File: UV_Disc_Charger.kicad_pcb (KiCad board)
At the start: 2 copper layers, 100 x 100 mm, 0 parts

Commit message: layout started
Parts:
- added C1: 10u, Capacitor_SMD:C_0805_2012Metric_Pad1.18x1.45mm_HandSolder, F.Cu at (242.0, 89.2)
- added C10: 100u, Capacitor_SMD:C_1206_3216Metric, F.Cu at (98.8, 170.2)
- added C11: 100n, Capacitor_SMD:C_0603_1608Metric_Pad1.08x0.95mm_HandSolder, F.Cu at (92.9, 173.8)
- added C2: 10u, Capacitor_SMD:C_0805_2012Metric_Pad1.18x1.45mm_HandSolder, F.Cu at (176.5, 76.2)
- added C3: 100n, Capacitor_SMD:C_0603_1608Metric_Pad1.08x0.95mm_HandSolder, F.Cu at (222.3, 86.4)
- added C4: 10u, Capacitor_SMD:C_0805_2012Metric, F.Cu at (98.2, 173.4)
- added C5: 10u, Capacitor_SMD:C_0805_2012Metric, F.Cu at (98.2, 176.4)
- added C6: 22u, Capacitor_SMD:C_1206_3216Metric, F.Cu at (98.8, 156.8)
- added C7: 22u, Capacitor_SMD:C_1206_3216Metric, F.Cu at (98.8, 160.2)
- added C8: 22u, Capacitor_SMD:C_1206_3216Metric, F.Cu at (98.8, 163.5)
- added C9: 22u, Capacitor_SMD:C_1206_3216Metric, F.Cu at (98.8, 166.9)
- added D1: SMBJ12CA, Diode_SMD:D_SMB, F.Cu at (167.6, 87.6)
- added D2: RED, Diode_SMD:D_0805_2012Metric, F.Cu at (185.4, 80.0)
- added D3: GREEN, Diode_SMD:D_0805_2012Metric, F.Cu at (183.5, 81.9)
- added D4: SS34, Diode_SMD:D_SMA, F.Cu at (163.8, 83.8)
- added F1: 1.5A, Fuse:Fuse_1206_3216Metric, F.Cu at (230.9, 51.4)
- added H1: MountingHole, MountingHole:MountingHole_3.2mm_M3_DIN965_Pad, F.Cu at (26.2, 109.8)
- added H2: MountingHole, MountingHole:MountingHole_3.2mm_M3_DIN965_Pad, F.Cu at (26.2, 117.0)
- added J1: Type-C_6P, Custom:USB-C 6 Pin - Long pads, F.Cu at (181.2, 91.1)
- added J2: JST PH Connector, Connector_JST:JST_PH_B2B-PH-K_1x02_P2.00mm_Vertical, F.Cu at (12.3, 133.7)
- added J3: Conn_01x01, Connector_PinHeader_2.54mm:PinHeader_1x01_P2.54mm_Vertical, F.Cu at (32.1, 108.5)
- added J4: JST PH Connector, Connector_JST:JST_PH_B2B-PH-K_1x02_P2.00mm_Vertical, F.Cu at (12.3, 140.3)
- added J5: JST PH Connector, Connector_PinHeader_2.54mm:PinHeader_1x02_P2.54mm_Vertical, F.Cu at (38.4, 122.8)
- added J6: JST PH Connector, Connector_PinHeader_2.54mm:PinHeader_1x02_P2.54mm_Vertical, F.Cu at (43.1, 122.8)
- added J7: Conn_01x01, Connector_PinHeader_2.54mm:PinHeader_1x01_P2.54mm_Vertical, F.Cu at (32.1, 113.2)
- added L1: 2u2, Custom:Combined CD43 + L 6.3x6.3, F.Cu at (105.5, 159.4)
- added Q1: SI2301, Package_TO_SOT_SMD:SOT-23, F.Cu at (237.5, 71.3)
- added Q2: SI2301, Package_TO_SOT_SMD:SOT-23, F.Cu at (243.0, 71.5)
- added R10: 1M6, Resistor_SMD:R_0805_2012Metric, F.Cu at (89.4, 148.2)
- added R11: 1M, Resistor_SMD:R_0805_2012Metric, F.Cu at (89.4, 151.2)
- added R12: 180k, Resistor_SMD:R_0805_2012Metric, F.Cu at (89.4, 154.1)
- added R13: 1k, Resistor_SMD:R_0805_2012Metric, F.Cu at (223.2, 57.4)
- added R14: 10k, Resistor_SMD:R_0805_2012Metric, F.Cu at (223.2, 60.3)
- added R15: 0R4, Resistor_SMD:R_0805_2012Metric, F.Cu at (174.0, 81.3)
- added R16: 2512 package, Resistor_SMD:R_2512_6332Metric, F.Cu at (174.0, 81.3)
- added R3: 100R, Resistor_SMD:R_0805_2012Metric, F.Cu at (214.3, 57.4)
- added R4: 1k, Resistor_SMD:R_0805_2012Metric, F.Cu at (181.0, 78.1)
- added R5: 1k, Resistor_SMD:R_0805_2012Metric, F.Cu at (214.3, 63.3)
- added R6: 5k1, Resistor_SMD:R_0805_2012Metric, F.Cu at (172.7, 94.0)
- added R7: 5k1, Resistor_SMD:R_0805_2012Metric, F.Cu at (170.2, 91.4)
- added R8: 1k, Resistor_SMD:R_0805_2012Metric, F.Cu at (182.9, 74.9)
- added R9: 2k, Resistor_SMD:R_0805_2012Metric, F.Cu at (185.4, 71.5)
- added U1: TP4056, Package_SO:SOP-8_3.76x4.96mm_P1.27mm, F.Cu at (179.1, 69.8)
- added U2: DW01A, Package_TO_SOT_SMD:SOT-23-6, F.Cu at (222.7, 82.9)
- added U3: FS8205A, Package_SO:TSSOP-8_4.4x3mm_P0.65mm, F.Cu at (241.5, 63.1)
- added U4: TPS63020, TPS63020:QFN14-3X4MM, F.Cu at (117.8, 166.3)
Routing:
- net Net-(D2-A): track 0.00 -> 31.4 mm
- net VBUS: track 0.00 -> 19.6 mm
- net Net-(D3-K): track 0.00 -> 13.7 mm
- net Net-(U1-CHRG): track 0.00 -> 10.4 mm, vias 0 -> 2
- net Net-(J1-CC2): track 0.00 -> 10.2 mm
- net Net-(J1-CC1): track 0.00 -> 10.0 mm
- net Net-(U1-STDBY): track 0.00 -> 9.66 mm, vias 0 -> 2
- net Net-(D2-K): track 0.00 -> 8.67 mm
- net Net-(U1-PROG): track 0.00 -> 3.84 mm
- net GND: track 0.00 -> 3.31 mm, vias 0 -> 2
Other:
- copper layers 2 -> 4

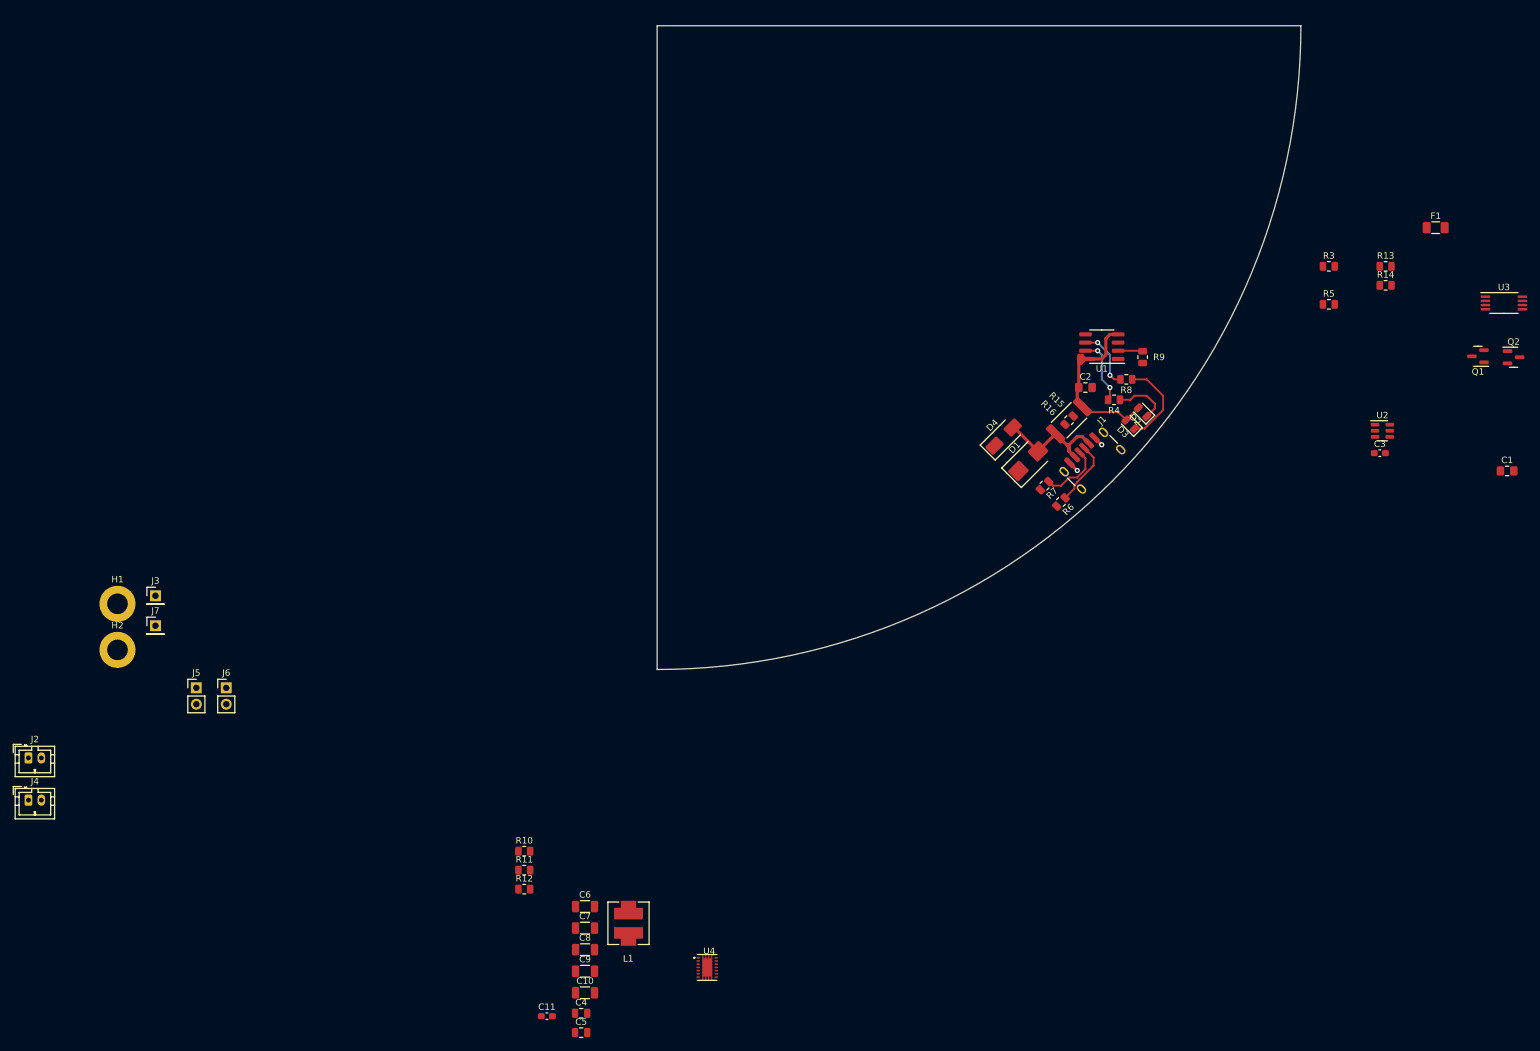
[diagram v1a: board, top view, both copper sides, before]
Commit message: added manufacturing files
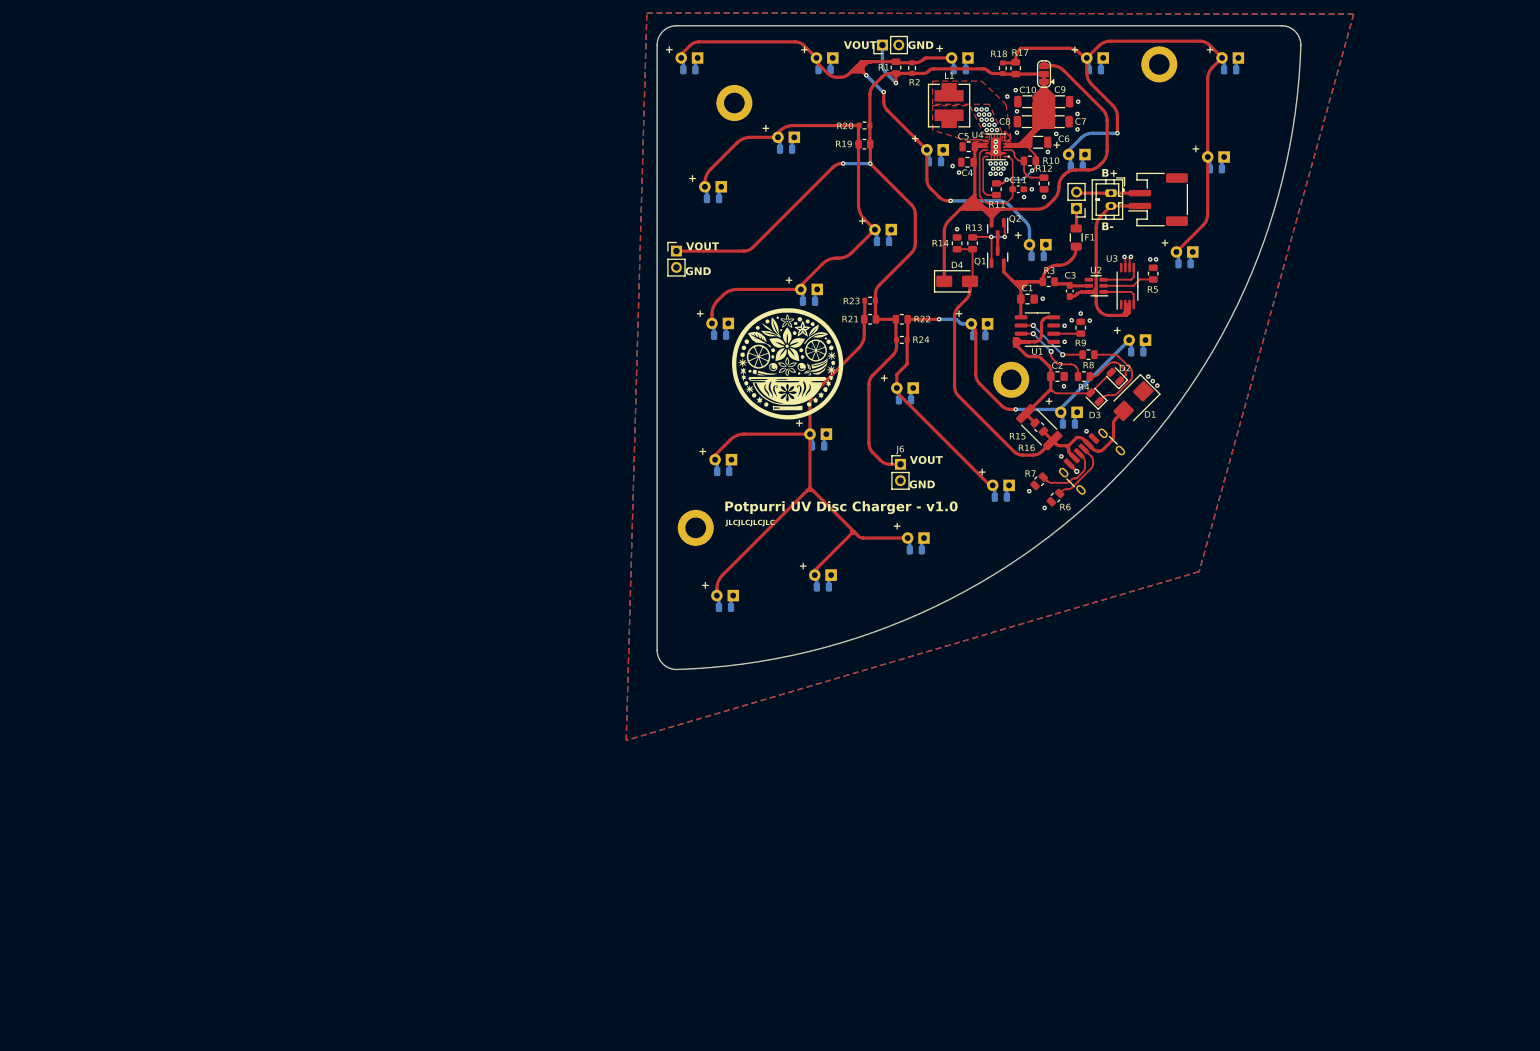
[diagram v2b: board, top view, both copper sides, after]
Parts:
- removed J7: Conn_01x01, Connector_PinHeader_2.54mm:PinHeader_1x01_P2.54mm_Vertical
- added D10: LED, Custom:LED-ThroughHole-And-SMD0805, B.Cu at (178.0, 25.0)
- added D11: LED, Custom:LED-ThroughHole-And-SMD0805, B.Cu at (199.0, 25.0)
- added D12: LED, Custom:LED-ThroughHole-And-SMD0805, B.Cu at (175.2, 40.0)
- added D13: LED, Custom:LED-ThroughHole-And-SMD0805, B.Cu at (196.8, 40.4)
- added D14: LED, Custom:LED-ThroughHole-And-SMD0805, B.Cu at (191.9, 55.1)
- added D15: LED, Custom:LED-ThroughHole-And-SMD0805, B.Cu at (118.7, 45.0)
- added D16: LED, Custom:LED-ThroughHole-And-SMD0805, B.Cu at (130.0, 37.3)
- added D17: LED, Custom:LED-ThroughHole-And-SMD0805, B.Cu at (119.8, 66.2)
- added D18: LED, Custom:LED-ThroughHole-And-SMD0805, B.Cu at (133.6, 61.0)
- added D19: LED, Custom:LED-ThroughHole-And-SMD0805, B.Cu at (145.1, 51.7)
- added D20: LED, Custom:LED-ThroughHole-And-SMD0805, B.Cu at (120.3, 87.4)
- added D21: LED, Custom:LED-ThroughHole-And-SMD0805, B.Cu at (160.1, 66.3)
- added D22: LED, Custom:LED-ThroughHole-And-SMD0805, B.Cu at (120.5, 108.5)
- added D23: LED, Custom:LED-ThroughHole-And-SMD0805, B.Cu at (174.0, 80.0)
- added D24: LED, Custom:LED-ThroughHole-And-SMD0805, B.Cu at (150.2, 99.6)
- added D25: LED, Custom:LED-ThroughHole-And-SMD0805, B.Cu at (148.5, 76.3)
- added D26: LED, Custom:LED-ThroughHole-And-SMD0805, B.Cu at (135.0, 83.4)
- added D27: LED, Custom:LED-ThroughHole-And-SMD0805, B.Cu at (163.4, 91.4)
- added D28: LED, Custom:LED-ThroughHole-And-SMD0805, B.Cu at (135.7, 105.3)
- added D29: LED, Custom:LED-ThroughHole-And-SMD0805, B.Cu at (184.6, 68.8)
- added D5: LED, Custom:LED-ThroughHole-And-SMD0805, B.Cu at (115.0, 25.0)
- added D6: LED, Custom:LED-ThroughHole-And-SMD0805, B.Cu at (136.0, 25.0)
- added D7: LED, Custom:LED-ThroughHole-And-SMD0805, B.Cu at (157.0, 25.0)
- added D8: LED, Custom:LED-ThroughHole-And-SMD0805, B.Cu at (153.2, 39.3)
- added D9: LED, Custom:LED-ThroughHole-And-SMD0805, B.Cu at (169.1, 54.0)
- added G***: LOGO, LOGO, F.Cu at (130.4, 72.5)
- added H3: MountingHole, MountingHole:MountingHole_3.2mm_M3_DIN965_Pad, F.Cu at (116.0, 98.0)
- added H4: MountingHole, MountingHole:MountingHole_3.2mm_M3_DIN965_Pad, F.Cu at (165.0, 75.0)
- added JP1: SolderJumper_3_Bridged12, Jumper:SolderJumper-3_P1.3mm_Bridged12_RoundedPad1.0x1.5mm, F.Cu at (170.1, 27.5)
- added R1: 0805, Resistor_SMD:R_0805_2012Metric, F.Cu at (147.1, 26.5)
- added R17: 0805, Resistor_SMD:R_0805_2012Metric, F.Cu at (165.7, 26.6)
- added R18: 0603, Resistor_SMD:R_0603_1608Metric, F.Cu at (163.7, 26.6)
- added R19: 0805, Resistor_SMD:R_0805_2012Metric, F.Cu at (142.2, 38.4)
- added R2: 0603, Resistor_SMD:R_0603_1608Metric, F.Cu at (149.6, 26.6)
- added R20: 0603, Resistor_SMD:R_0603_1608Metric, F.Cu at (142.2, 35.5)
- added R21: 0805, Resistor_SMD:R_0805_2012Metric, F.Cu at (143.1, 65.6)
- added R22: 0805, Resistor_SMD:R_0805_2012Metric, F.Cu at (148.0, 65.6)
- added R23: 0603, Resistor_SMD:R_0603_1608Metric, F.Cu at (143.1, 62.7)
- added R24: 0603, Resistor_SMD:R_0603_1608Metric, F.Cu at (148.0, 68.8)
- added SW1: SW_SPST, Connector_PinHeader_2.54mm:PinHeader_1x02_P2.54mm_Vertical, F.Cu at (175.2, 48.4)
- J3: value Conn_01x01 -> Connector; footprint Connector_PinHeader_2.54mm:PinHeader_1x01_P2.54mm_Vertical -> Connector_PinHeader_2.54mm:PinHeader_1x02_P2.54mm_Vertical
- J4: footprint Connector_JST:JST_PH_B2B-PH-K_1x02_P2.00mm_Vertical -> Connector_JST:JST_PH_S2B-PH-SM4-TB_1x02-1MP_P2.00mm_Horizontal
- J5, J6: value JST PH Connector -> Connector
- moved J4 198.8 mm to (187.8, 47.0), turned to 90 degrees
- moved J2 189.7 mm to (180.5, 46.0), turned to -90 degrees
- moved H2 185.6 mm to (188.0, 26.0)
- moved C10 154.5 mm to (167.5, 31.8), turned to 180 degrees
- moved C9 153.9 mm to (172.6, 31.8)
- moved C5 150.2 mm to (158.4, 38.8), turned to 180 degrees
- moved C11 147.9 mm to (166.1, 45.4)
- moved C8 145.8 mm to (167.4, 34.9), turned to 180 degrees
- moved C7 145.4 mm to (172.5, 34.9)
- moved C4 145.2 mm to (158.2, 41.2), turned to 180 degrees
- moved J3 141.7 mm to (145.0, 23.0), turned to 90 degrees
- moved C6 138.0 mm to (169.2, 38.1)
- moved L1 136.5 mm to (155.4, 32.4), turned to 180 degrees
- moved R12 136.1 mm to (170.1, 44.5), turned to -90 degrees
- moved U4 135.1 mm to (162.6, 38.8), turned to 180 degrees
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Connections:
- F1 pad 1: +BATT -> Net-(SW1-A)
- J3 pad 1: +BATT -> +VSW
- J4 pad 1: +5V -> -BATT
- J4 pad 2: GND -> +BATT
- J5 pad 1: GND -> +VSW
- J6 pad 1: +5V -> +VSW
- J6 pad 2: +5V -> GND
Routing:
- net +VSW: track 0.00 -> 143.5 mm, vias 0 -> 3
- net +5V: track 0.00 -> 128.1 mm, vias 0 -> 2
- net Net-(D5-A): track 0.00 -> 113.1 mm, vias 0 -> 3
- net Net-(D20-A): track 0.00 -> 111.6 mm
- net Net-(D10-A): track 0.00 -> 103.5 mm, vias 0 -> 1
- net VCC: track 0.00 -> 99.9 mm
- net Net-(D21-A): track 0.00 -> 92.5 mm, vias 0 -> 2
- net Net-(D15-A): track 0.00 -> 88.7 mm
- net GND: track 3.31 -> 62.2 mm, vias 2 -> 62
- net VBUS: track 19.6 -> 67.6 mm
- net -BATT: track 0.00 -> 39.7 mm
- net Net-(Q1-S): track 0.00 -> 30.4 mm
- net Net-(U4-EN): track 0.00 -> 21.0 mm
- net Net-(D2-A): track 31.4 -> 43.0 mm
- net Net-(Q1-G): track 0.00 -> 11.4 mm, vias 0 -> 2
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- added copper zone on B.Cu, net GND
- added copper zone on F.Cu, net GND
- added copper zone on F.Cu, net Net-(L1-Pad1)
- added copper zone on F.Cu, net Net-(L1-Pad2)
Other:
- outline, holes or cut-outs redrawn
- copper layers 4 -> 2
- board text added: "+"
- board text added: "B+"
- board text added: "B-"
- board text added: "GND"
- board text added: "JLCJLCJLCJLC"
- board text added: "Potpurri UV Disc Charger - v1.0"
- board text added: "VOUT"
